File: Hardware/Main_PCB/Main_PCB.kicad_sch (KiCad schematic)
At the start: 6 parts, among them J101 Conn_01x08_Pin, J102 Conn_01x03_Pin, U101 NRF24L01_Breakout, U9 SN74LV1T34DBV

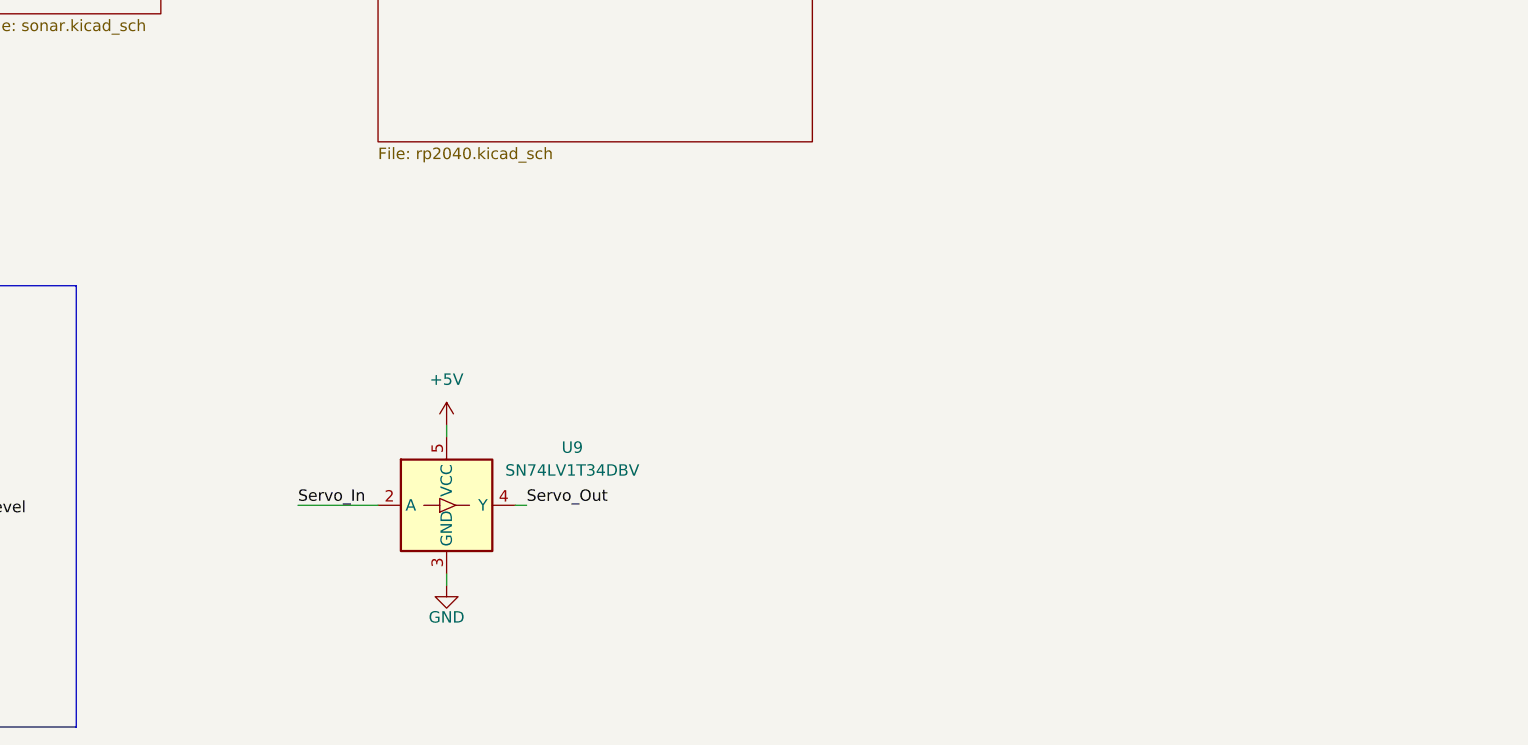
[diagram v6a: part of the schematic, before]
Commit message: Updated Main_PCB.kicad_sch with servo connector
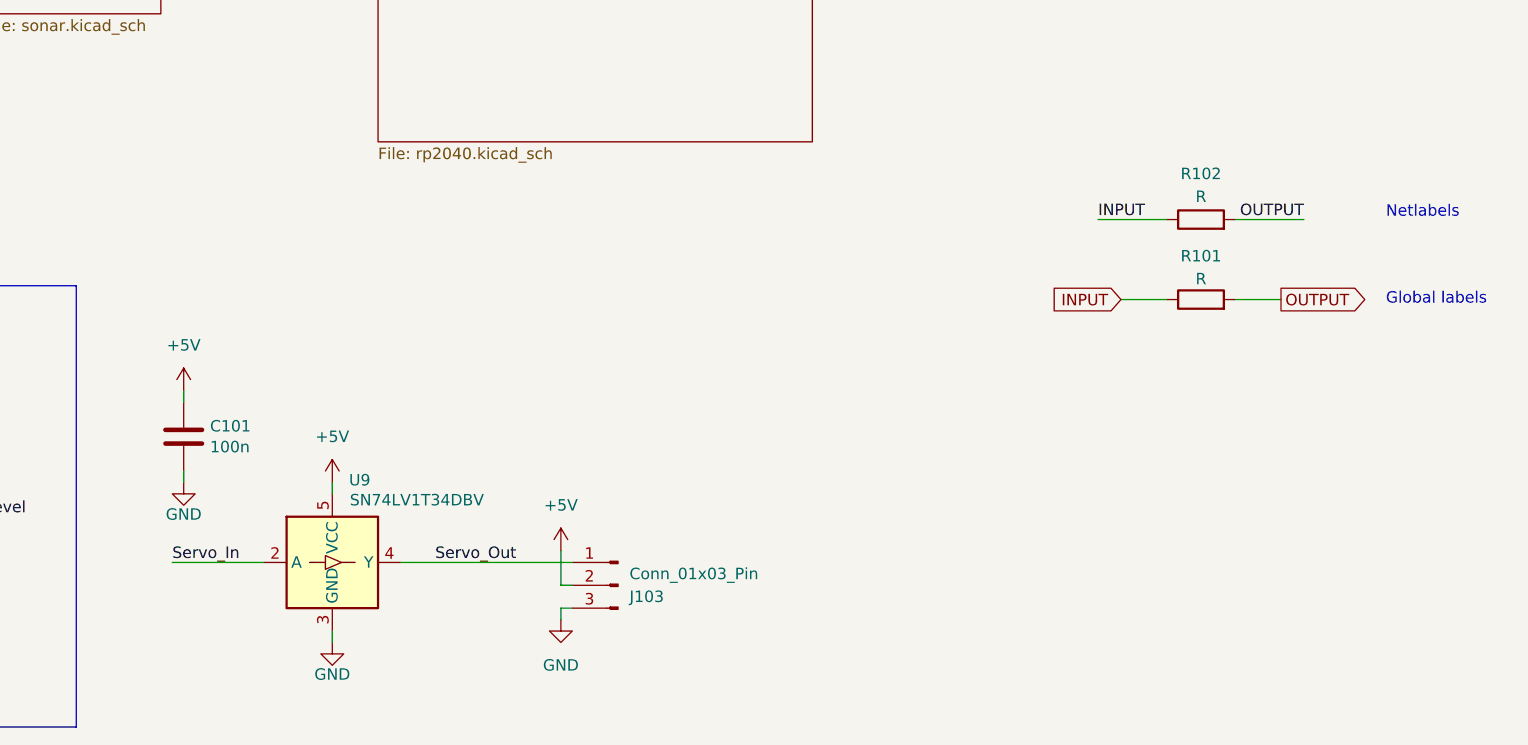
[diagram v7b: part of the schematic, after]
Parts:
- added C101: 100n, Capacitor_SMD:C_0603_1608Metric_Pad1.08x0.95mm_HandSolder, symbol Device:C
- added J103: Conn_01x03_Pin, Connector_JST:JST_PH_B3B-PH-K_1x03_P2.00mm_Vertical, symbol Connector:Conn_01x03_Pin
- added R101, R102: R, symbol Device:R
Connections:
- net +5V: now also C101.1, J103.2 (Pin_2)
- net GND: now also C101.2, J103.3 (Pin_3)
- net Servo_Out: now also J103.1 (Pin_1)
- new net INPUT: R101.1, R102.1
- new net OUTPUT: R101.2, R102.2
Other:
- note added: "Global labels"
- note added: "Netlabels"
- moved on the sheet: U9

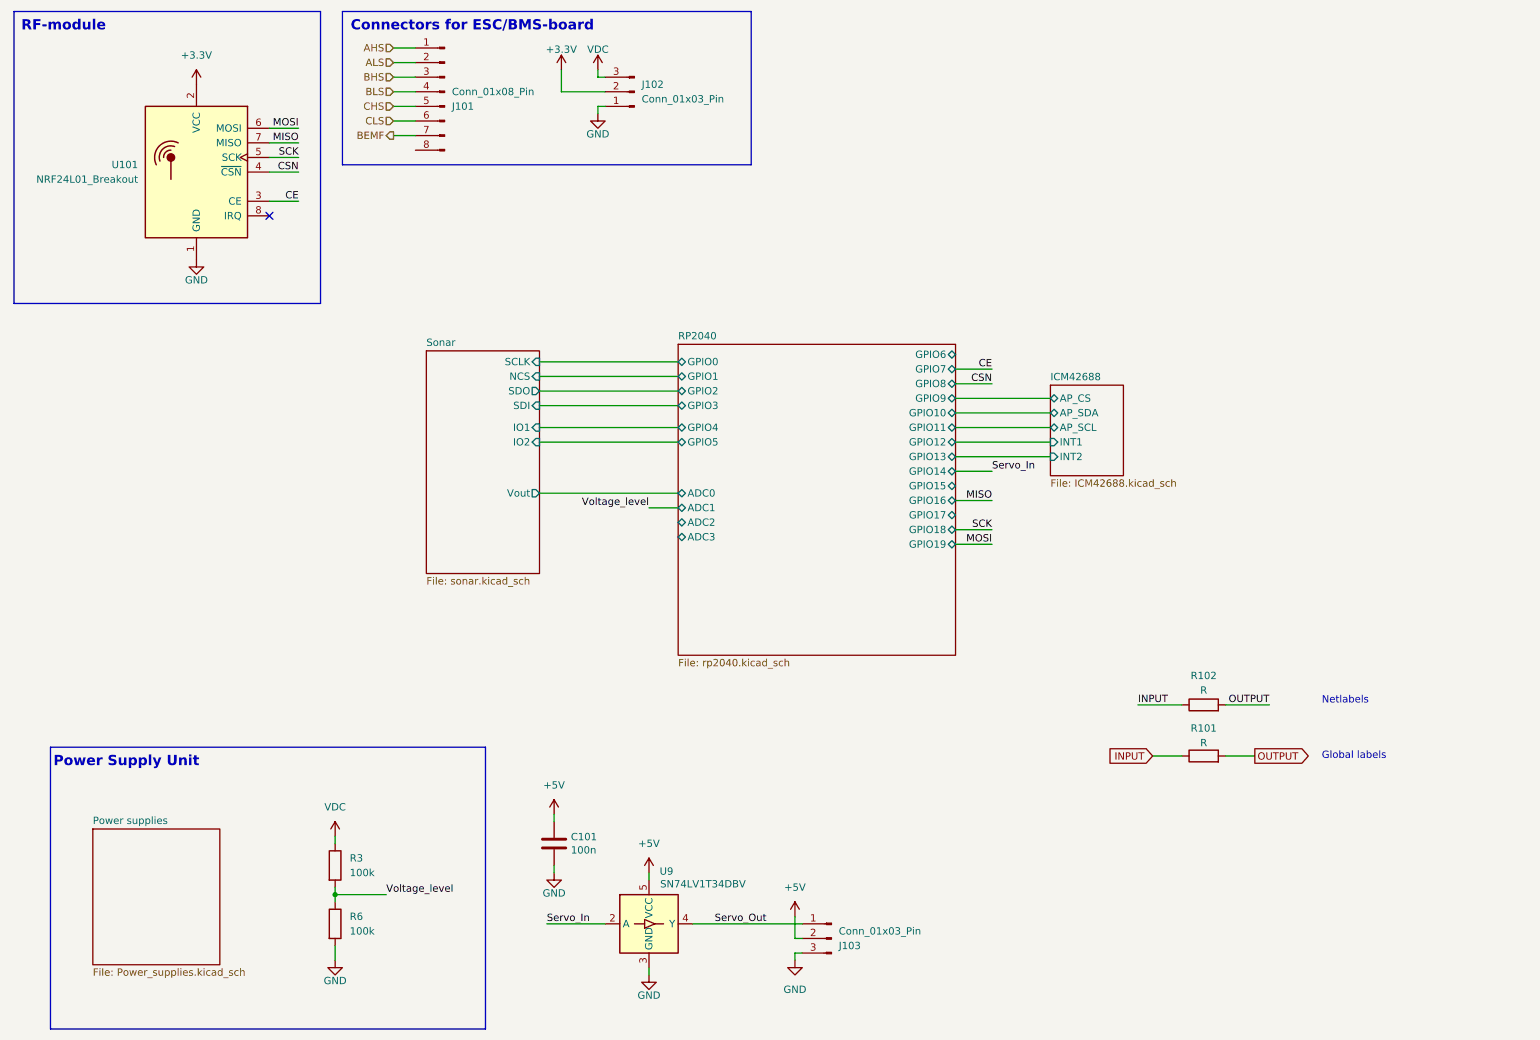
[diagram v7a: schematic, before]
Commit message: A finished version of the Main PCB schematic
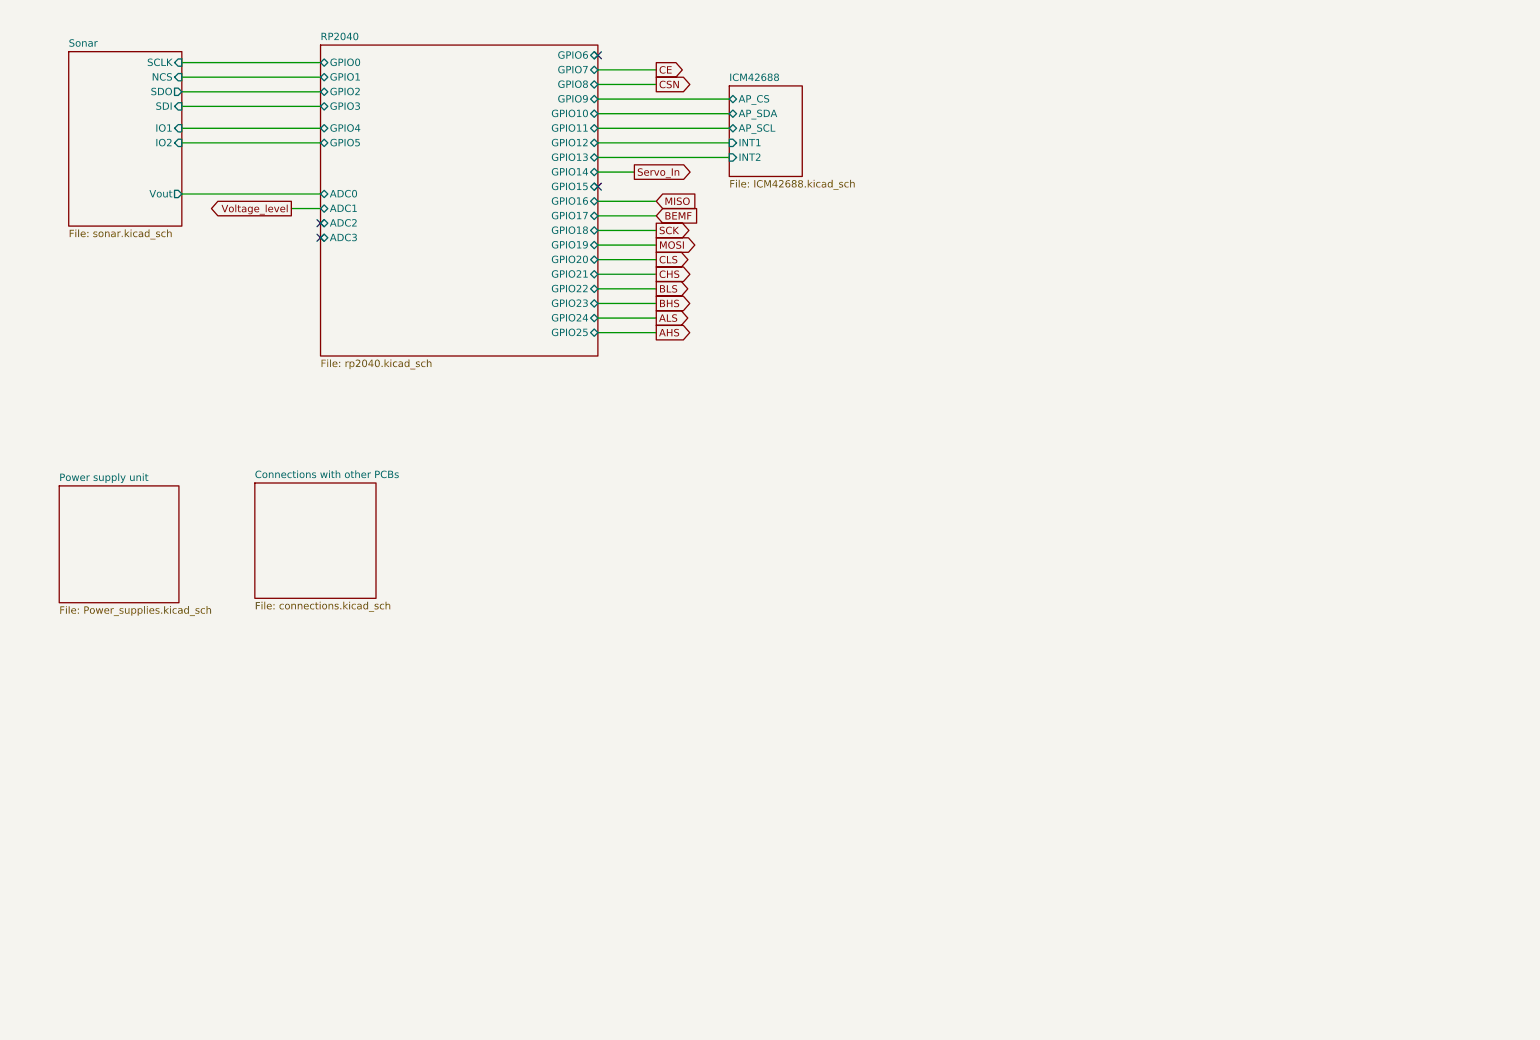
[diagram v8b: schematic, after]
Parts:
- removed C101: 100n, Capacitor_SMD:C_0603_1608Metric_Pad1.08x0.95mm_HandSolder, symbol Device:C
- removed J101: Conn_01x08_Pin, Connector_JST:JST_PH_B8B-PH-K_1x08_P2.00mm_Vertical, symbol Connector:Conn_01x08_Pin
- removed J102, J103: Conn_01x03_Pin, Connector_JST:JST_PH_B3B-PH-K_1x03_P2.00mm_Vertical, symbol Connector:Conn_01x03_Pin
- removed R101, R102: R, symbol Device:R
- removed R3, R6: 100k, Resistor_SMD:R_0603_1608Metric_Pad0.98x0.95mm_HandSolder, symbol Device:R
- removed U101: NRF24L01_Breakout, RF_Module:nRF24L01_Breakout, symbol RF:NRF24L01_Breakout
- removed U9: SN74LV1T34DBV, Package_TO_SOT_SMD:SOT-23-5, symbol Logic_LevelTranslator:SN74LV1T34DBV
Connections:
- no-connect marks 1 -> 4
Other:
- sheet Power supplies renamed Power supply unit
- added sheet Connections with other PCBs (connections.kicad_sch)
- sheet RP2040 ports: added GPIO20, GPIO21, GPIO22, GPIO23, GPIO24, GPIO25; removed none
- note removed: "Connectors for ESC/BMS-board"
- note removed: "Global labels"
- note removed: "Netlabels"
- note removed: "Power Supply Unit"
- note removed: "RF-module"
